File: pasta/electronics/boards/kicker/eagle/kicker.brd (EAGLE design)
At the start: 113.5 x 69.4 mm, 89 parts, among them Q101 FJT44TF, Q102 TPH3300CNH, Q201 IXYT55N120A4HV, Q202 IXYT55N120A4HV, T101 WE_FB_EFD25-750310988, U101 LT3748IMS, U201 UCC27532, U202 UCC27532, U203 NCP785AH150T1G, U204 NCP785AH150T1G, U301 AMC1304L05DWDW0016B_HV, Y301 DSC1123CI2-020.0000

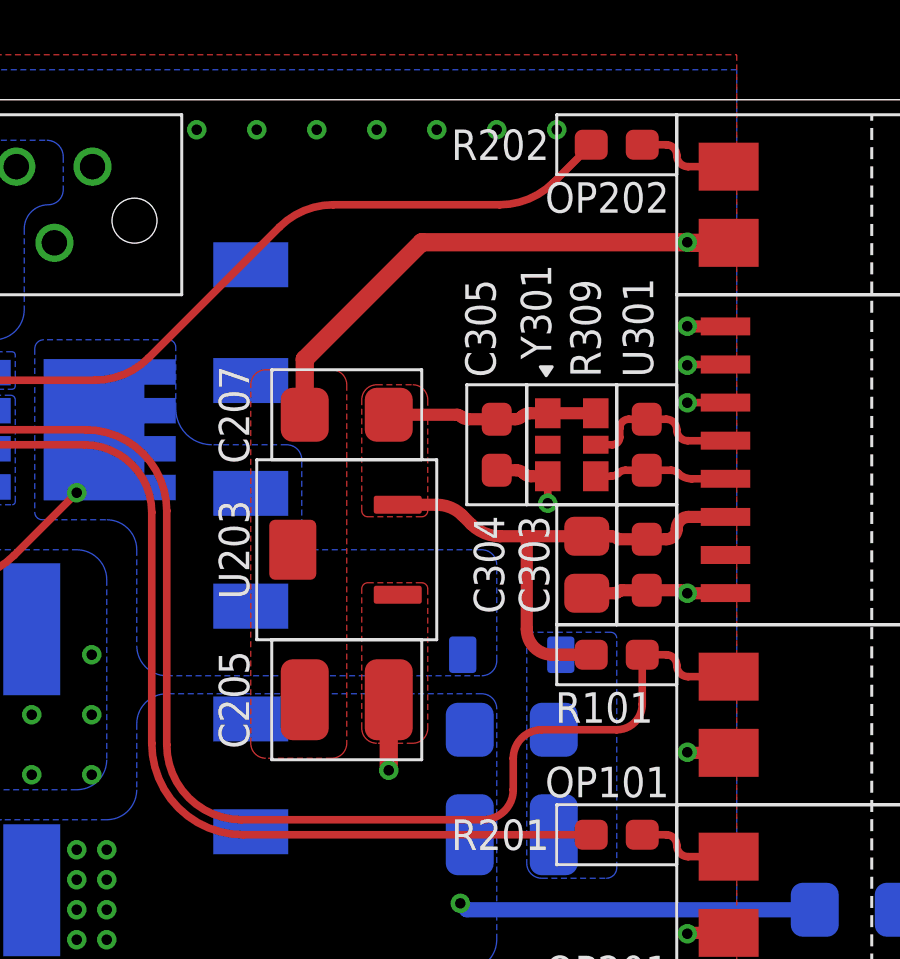
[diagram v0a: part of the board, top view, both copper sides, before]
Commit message: pasta: kicker: fix some bugs in schematics
- U203 had the wrong MPN (now replaced by a 3V3 LDO)
- Increased input capacitor of U203 to 10u 50V (previously 330n 250V)
- Changed title of U203 block in schematics to be more fitting
- Fixed MPN of optocouplers (value was right, but MPN was wrong)
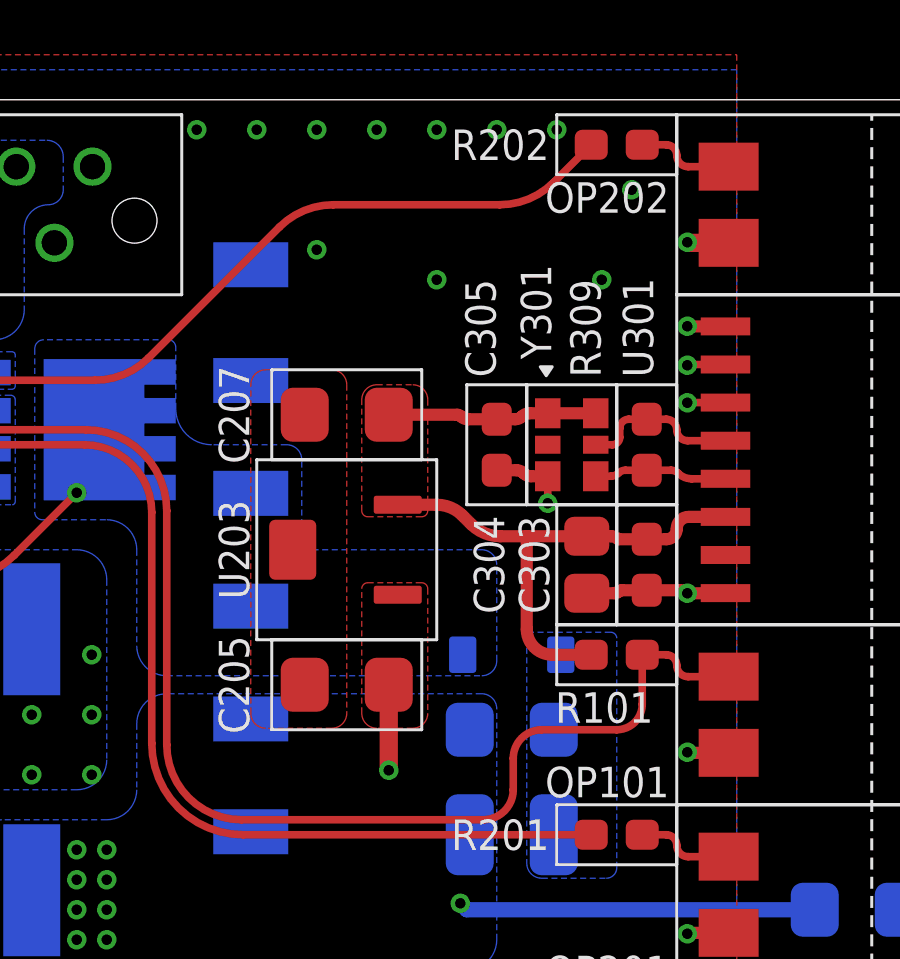
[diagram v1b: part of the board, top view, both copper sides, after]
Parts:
- C205: value (none) -> 10u ±20% 50V X5R; device capacitors:C1210 -> capacitors:C1206
- OP101, OP201, OP202: value LTV352T -> LTV-352T
- U203: value NCP785AH150T1G -> NCP785AH33T1G
- moved C205 0.50 mm to (11.0, -4.50)
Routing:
- net GND: track 60.3 -> 44.1 mm, vias 81 -> 85
- net VCC: track 14.3 -> 14.8 mm
